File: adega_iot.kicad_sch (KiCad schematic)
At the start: 38 parts, among them J1 Screw_Terminal_01x02, J2 Conn_01x02_Pin, J3 Conn_01x02_Pin, J4 Conn_01x03_Pin, J5 Conn_01x02_Pin, J6 Conn_01x03_Pin, J7 Screw_Terminal_01x02, Q1 IRF540N, Q10 BC548, Q11 BC558, Q2 IRF540N, Q3 BC548, Q4 BC558, Q5 BC548, Q6 BC548, Q7 BC548, Q8 BC558, Q9 BC548, SW1 SW_Push, SW2 SW_Push, U1 RC4558, U2 ESP32-DevKitC

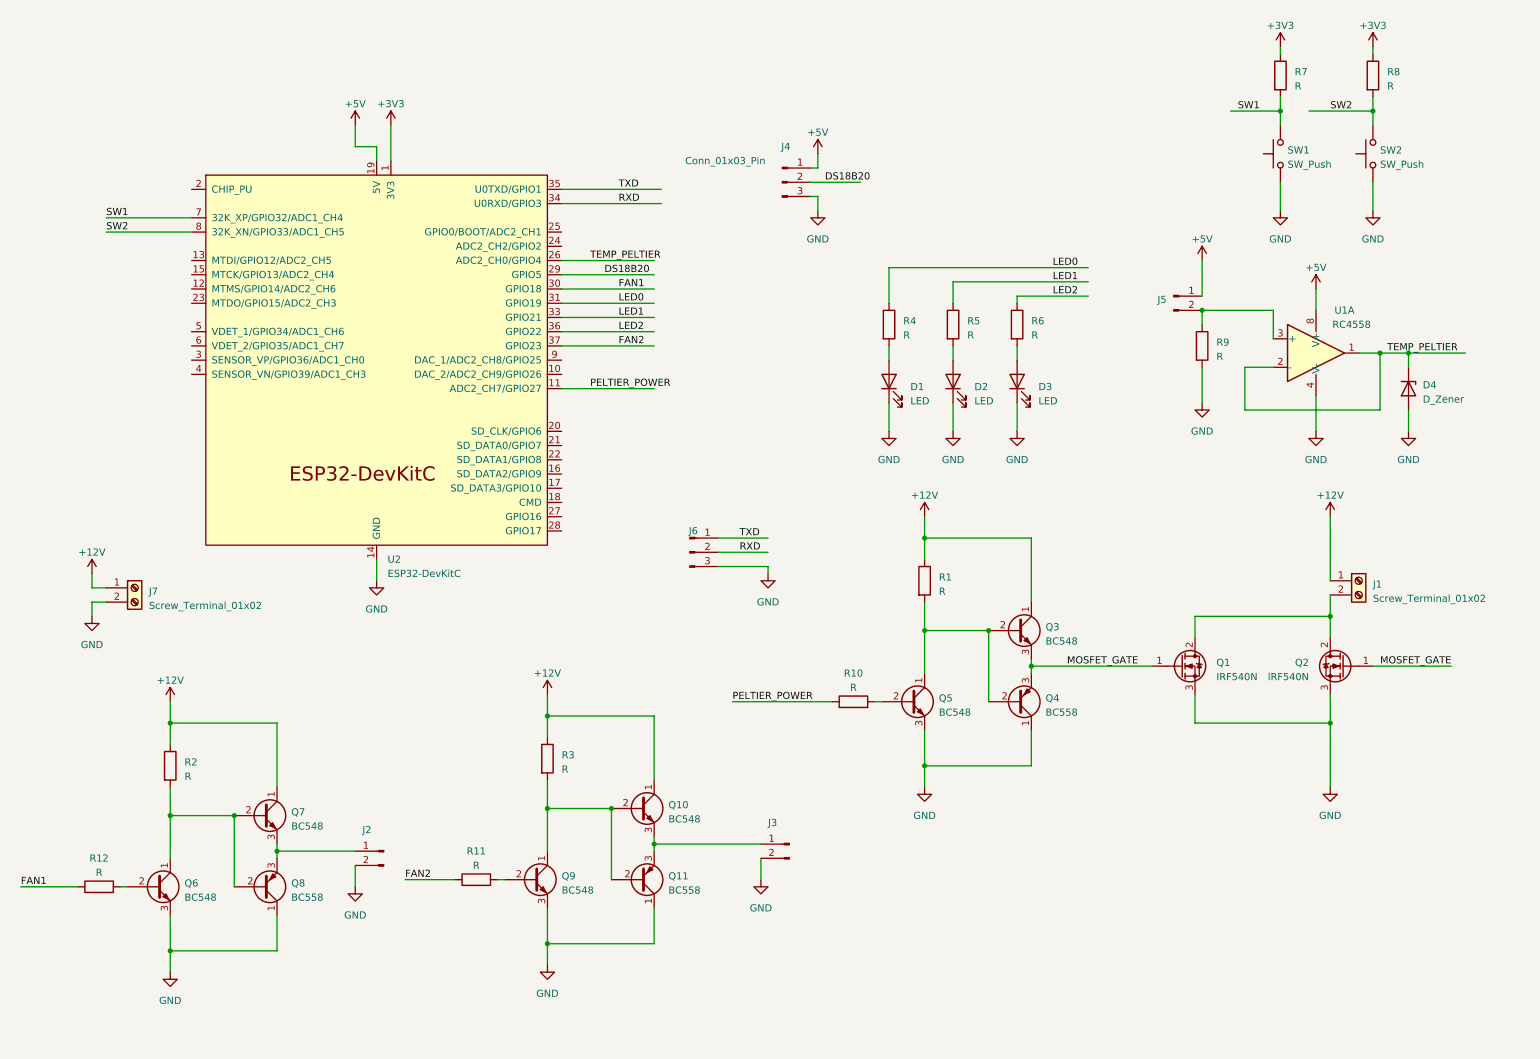
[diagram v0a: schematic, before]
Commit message: Added LM2596
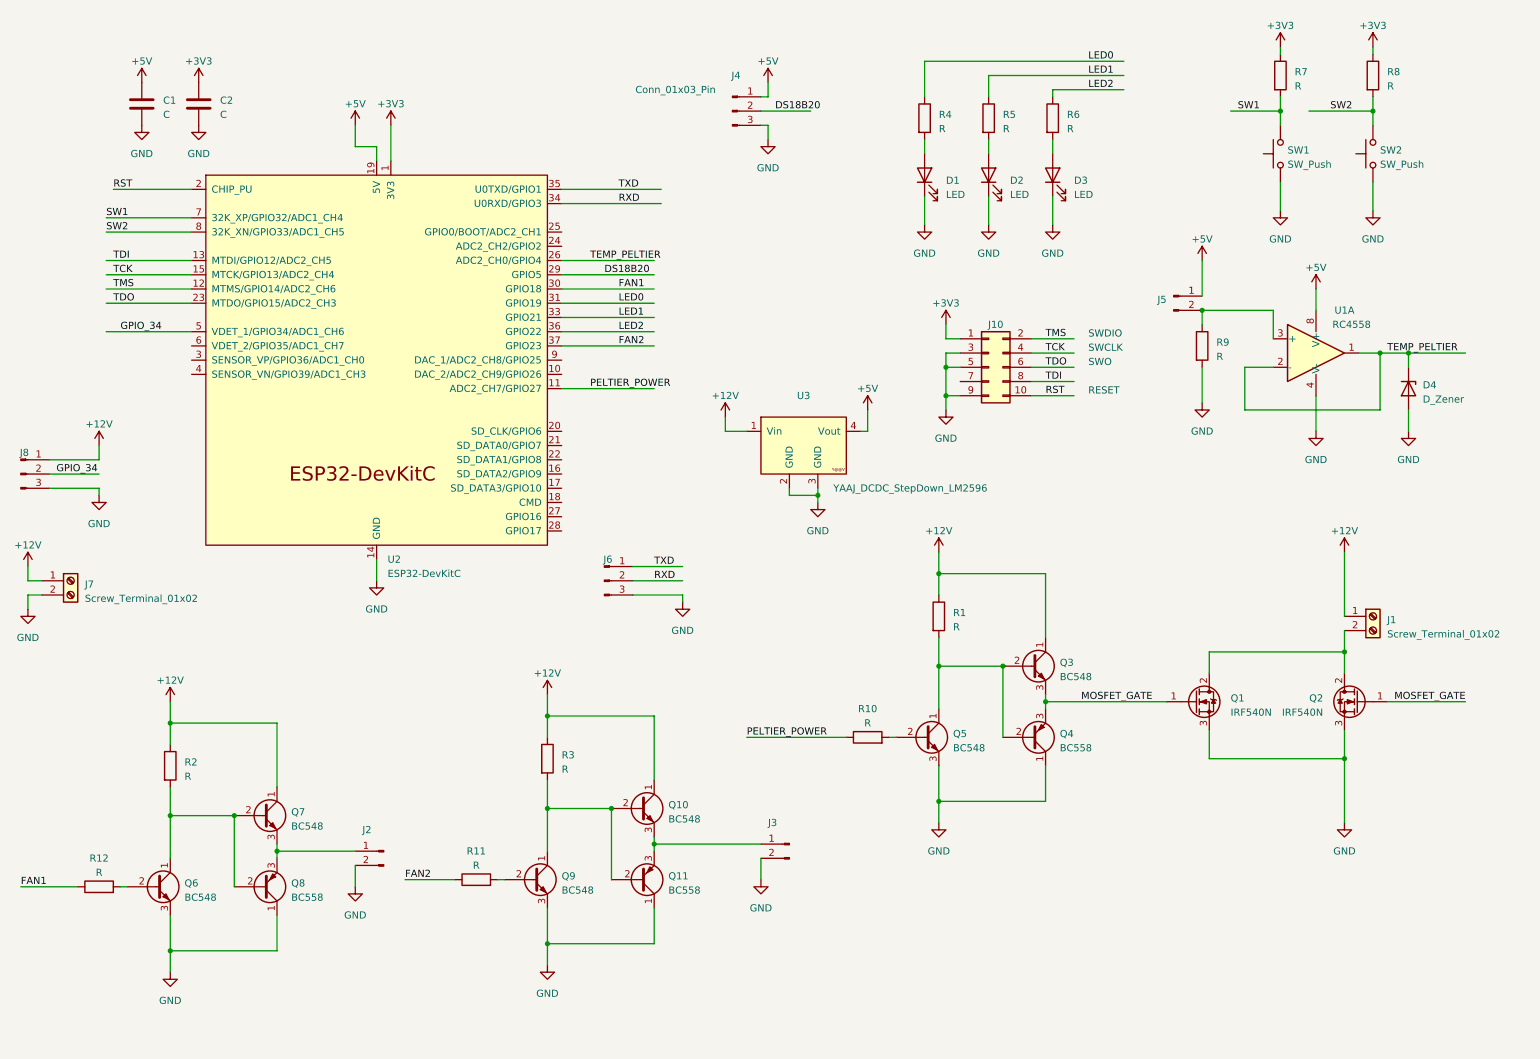
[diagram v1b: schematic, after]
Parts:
- added C1, C2: C, symbol Device:C
- added J10: Conn_02x05_Odd_Even, symbol Connector_Generic:Conn_02x05_Odd_Even
- added J8: Conn_01x03_Pin, symbol Connector:Conn_01x03_Pin
- added U3: YAAJ_DCDC_StepDown_LM2596, lm2596:YAAJ_DCDC_StepDown_LM2596, symbol lm2596:YAAJ_DCDC_StepDown_LM2596
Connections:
- net +12V: now also J8.1 (Pin_1), U3.1 (Vin)
- net +3V3: now also C2.1, J10.1 (Pin_1)
- net +5V: now also C1.1, U3.4 (Vout)
- net GND: now also C1.2, C2.2, J10.3 (Pin_3), J10.5 (Pin_5), J10.9 (Pin_9), J8.3 (Pin_3), U3.2 (GND), U3.3 (GND)
- net TMS: now reaches U2.12 (MTMS/GPIO14/ADC2_CH6)
- net TMS: now also J10.2 (Pin_2)
- net TDI: now reaches U2.13 (MTDI/GPIO12/ADC2_CH5)
- net TDI: now also J10.8 (Pin_8)
- net TCK: now reaches U2.15 (MTCK/GPIO13/ADC2_CH4)
- net TCK: now also J10.4 (Pin_4)
- net RST: now reaches U2.2 (CHIP_PU)
- net RST: now also J10.10 (Pin_10)
- net TDO: now reaches U2.23 (MTDO/GPIO15/ADC2_CH3)
- net TDO: now also J10.6 (Pin_6)
- net GPIO_34: now reaches U2.5 (VDET_1/GPIO34/ADC1_CH6)
- net GPIO_34: now also J8.2 (Pin_2)
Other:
- note added: "RESET"
- note added: "SWCLK"
- note added: "SWDIO"
- note added: "SWO"
- moved on the sheet: D1, D2, D3, J1, J4, J6, J7, Q1, Q2, Q3, Q4, Q5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

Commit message: adding screw terminals
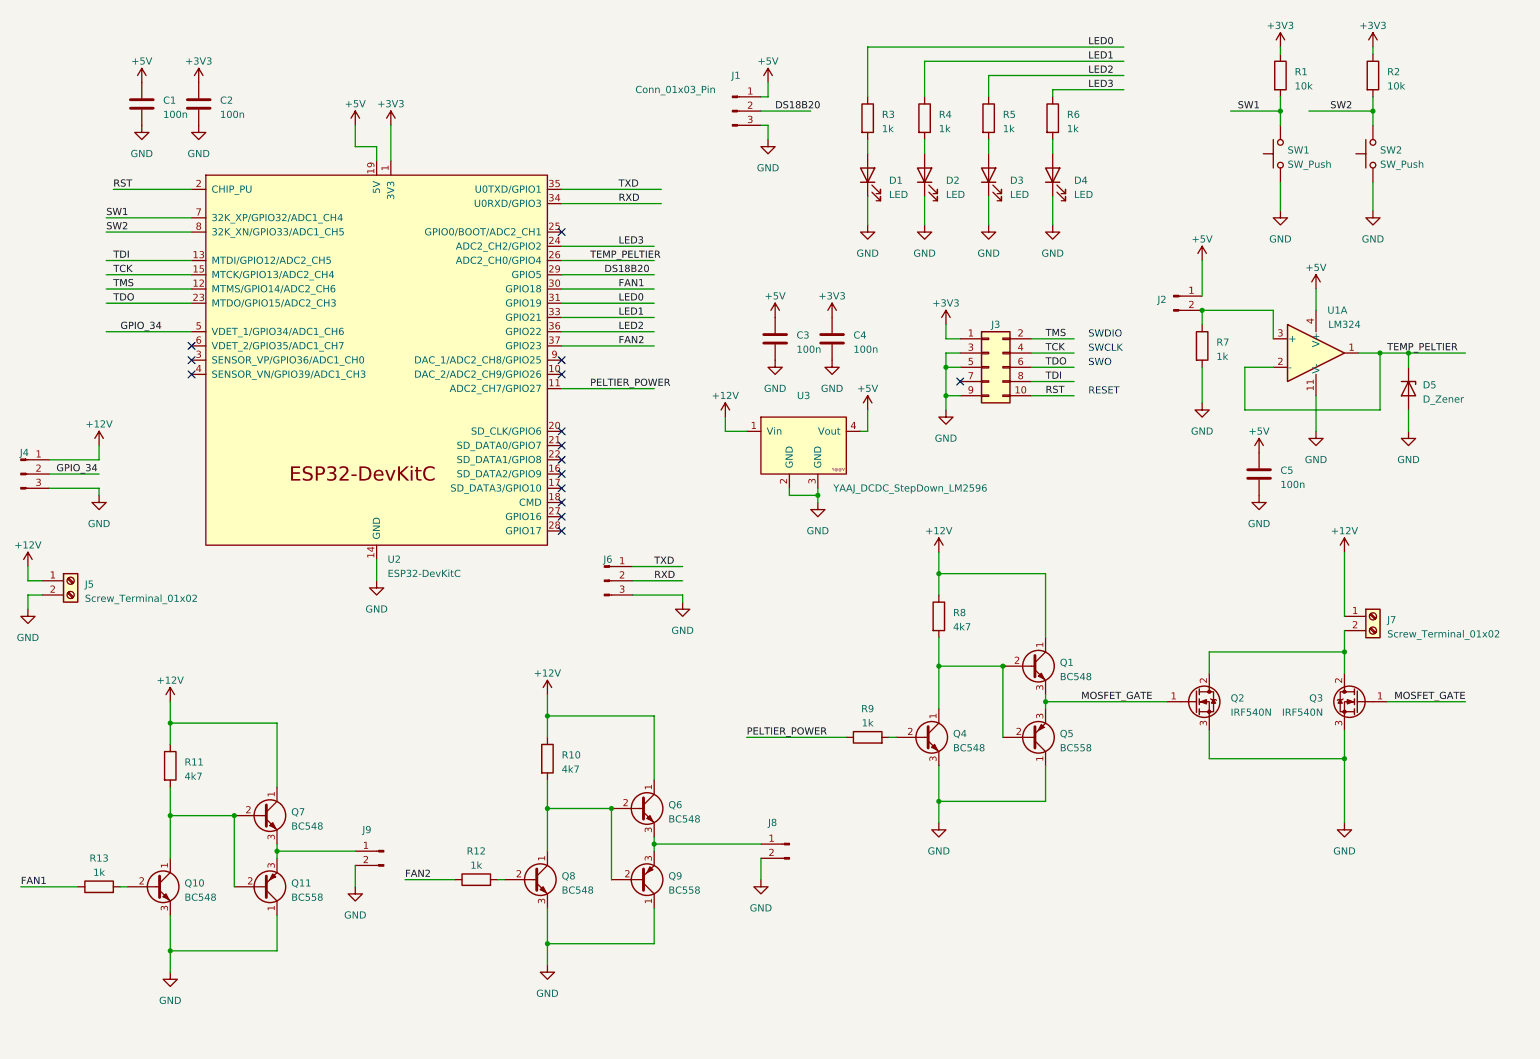
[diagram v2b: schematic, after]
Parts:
- removed U1: RC4558, symbol Amplifier_Operational:RC4558
- added C3, C4, C5: 100n, Capacitor_THT:C_Disc_D7.5mm_W4.4mm_P5.00mm, symbol Device:C
- added D1: LED, LED_THT:LED_D3.0mm, symbol Device:LED
- added R3: 1k, Resistor_THT:R_Axial_DIN0204_L3.6mm_D1.6mm_P7.62mm_Horizontal, symbol Device:R
- added U1: LM324, Package_DIP:DIP-14_W7.62mm, symbol Amplifier_Operational:LM324
- C1, C2: value C -> 100n; footprint (none) -> Capacitor_THT:C_Disc_D7.5mm_W4.4mm_P5.00mm
- D2: renamed from D1; footprint (none) -> LED_THT:LED_D3.0mm
- D3: renamed from D2; footprint (none) -> LED_THT:LED_D3.0mm
- D4: renamed from D3; footprint (none) -> LED_THT:LED_D3.0mm
- D5: renamed from D4; footprint (none) -> Diode_THT:D_A-405_P7.62mm_Horizontal
- J1: renamed from J4; footprint (none) -> Connector_PinHeader_2.54mm:PinHeader_1x03_P2.54mm_Vertical
- J2: renamed from J5; footprint (none) -> Connector_PinHeader_2.54mm:PinHeader_1x02_P2.54mm_Vertical
- J3: renamed from J10; footprint (none) -> Connector_PinHeader_2.54mm:PinHeader_2x05_P2.54mm_Vertical
- J4: renamed from J8; footprint (none) -> Connector_PinHeader_2.54mm:PinHeader_1x03_P2.54mm_Vertical
- J6: footprint (none) -> Connector_PinHeader_2.54mm:PinHeader_1x03_P2.54mm_Vertical
- R1: renamed from R7; value R -> 10k; footprint (none) -> Resistor_THT:R_Axial_DIN0204_L3.6mm_D1.6mm_P7.62mm_Horizontal
- R10: renamed from R3; value R -> 4k7; footprint (none) -> Resistor_THT:R_Axial_DIN0204_L3.6mm_D1.6mm_P7.62mm_Horizontal
- R11: renamed from R2; value R -> 4k7; footprint (none) -> Resistor_THT:R_Axial_DIN0204_L3.6mm_D1.6mm_P7.62mm_Horizontal
- R12: renamed from R11; value R -> 1k; footprint (none) -> Resistor_THT:R_Axial_DIN0204_L3.6mm_D1.6mm_P7.62mm_Horizontal
- R13: renamed from R12; value R -> 1k; footprint (none) -> Resistor_THT:R_Axial_DIN0204_L3.6mm_D1.6mm_P7.62mm_Horizontal
- R2: renamed from R8; value R -> 10k; footprint (none) -> Resistor_THT:R_Axial_DIN0204_L3.6mm_D1.6mm_P7.62mm_Horizontal
- R4, R5, R6: value R -> 1k; footprint (none) -> Resistor_THT:R_Axial_DIN0204_L3.6mm_D1.6mm_P7.62mm_Horizontal
- R7: renamed from R9; value R -> 1k; footprint (none) -> Resistor_THT:R_Axial_DIN0204_L3.6mm_D1.6mm_P7.62mm_Horizontal
- R8: renamed from R1; value R -> 4k7; footprint (none) -> Resistor_THT:R_Axial_DIN0204_L3.6mm_D1.6mm_P7.62mm_Horizontal
- R9: renamed from R10; value R -> 1k; footprint (none) -> Resistor_THT:R_Axial_DIN0204_L3.6mm_D1.6mm_P7.62mm_Horizontal
- renumbered J7 to J5, J1 to J7, J3 to J8, J2 to J9, Q3 to Q1, Q6 to Q10, Q8 to Q11, Q1 to Q2, Q2 to Q3, Q5 to Q4, Q4 to Q5, Q10 to Q6, Q9 to Q8, Q11 to Q9
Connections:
- net +3V3: now also C4.1
- net +5V: now also C3.1, C5.1, U1.4 (V+)
- net GND: now also C3.2, C4.2, C5.2, D1.1 (K), U1.11 (V-)
- net LED0: now also R3.1; no longer R4.1
- net LED1: now also R4.1; no longer R5.1
- net LED2: now also R5.1; no longer R6.1
- net TEMP_PELTIER: now also U1.1, U1.2 (-)
- net at J2.2 (Pin_2), R7.1: now also U1.3 (+)
- net LED3: now reaches U2.24 (ADC2_CH2/GPIO2)
- net LED3: now also R6.1
- new net: D1.2 (A), R3.2
- no-connect marks 0 -> 15

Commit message: Preliminary placement
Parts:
- added F1: Fuse, adega_iot:Metaltex_fuse_holder, symbol Device:Fuse
- J5, J7: footprint (none) -> adega_iot:HANDSON_KF301-2P
- J8, J9: footprint (none) -> Connector_PinHeader_2.54mm:PinHeader_1x02_P2.54mm_Vertical
- Q1, Q10, Q11, Q4, Q5, Q6, Q7, Q8, Q9: footprint Package_TO_SOT_THT:TO-92_Inline -> Package_TO_SOT_THT:TO-92_Inline_Wide
- SW1, SW2: footprint (none) -> Button_Switch_THT:SW_PUSH_6mm_H7.3mm
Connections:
- net +12V: now also F1.1; no longer J5.1 (Pin_1)
- net +3V3: no longer C4.1
- net +5V: now also C4.1
- new net: F1.2, J5.1 (Pin_1)
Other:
- moved on the sheet: C4, J5

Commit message: partial routing
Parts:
- removed C5: 100n, Capacitor_THT:C_Disc_D7.5mm_W4.4mm_P5.00mm, symbol Device:C
- added H1, H10, H11, H12, H2, H3, H4, H5, H6, H7, H8, H9: MountingHole, MountingHole:MountingHole_2mm, symbol Mechanical:MountingHole
- added H13, H14, H15, H16: MountingHole, MountingHole:MountingHole_3.2mm_M3, symbol Mechanical:MountingHole
- added J10: Conn_01x02_Pin, Connector_PinHeader_2.54mm:PinHeader_1x02_P2.54mm_Vertical, symbol Connector:Conn_01x02_Pin
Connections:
- net DS18B20: now also U2.31 (GPIO19); no longer U2.29 (GPIO5)
- net FAN1: now also U2.24 (ADC2_CH2/GPIO2); no longer U2.30 (GPIO18)
- net FAN2: now also U2.29 (GPIO5); no longer U2.37 (GPIO23)
- net GND: now also J10.2 (Pin_2)
- net LED0: now also U2.5 (VDET_1/GPIO34/ADC1_CH6); no longer U2.31 (GPIO19)
- net LED1: now also U2.6 (VDET_2/GPIO35/ADC1_CH7); no longer U2.33 (GPIO21)
- net LED2: now also U2.7 (32K_XP/GPIO32/ADC1_CH4); no longer U2.36 (GPIO22)
- net LED3: now also U2.8 (32K_XN/GPIO33/ADC1_CH5); no longer U2.24 (ADC2_CH2/GPIO2)
- net SW1: now also U2.10 (DAC_2/ADC2_CH9/GPIO26); no longer U2.7 (32K_XP/GPIO32/ADC1_CH4)
- net SW2: now also U2.9 (DAC_1/ADC2_CH8/GPIO25); no longer U2.8 (32K_XN/GPIO33/ADC1_CH5)
- net BOOT: now reaches U2.25 (GPIO0/BOOT/ADC2_CH1)
- net BOOT: now also J10.1 (Pin_1)
- net GPIO_16: now reaches U2.27 (GPIO16)
- net GPIO_16: now also J4.2 (Pin_2)
- removed net GPIO_34: J4.2 (Pin_2), U2.5 (VDET_1/GPIO34/ADC1_CH6)
- no-connect marks 15 -> 8

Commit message: Routing Progress
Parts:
- removed D5: D_Zener, Diode_THT:D_A-405_P7.62mm_Horizontal, symbol Device:D_Zener
- removed J3: Conn_02x05_Odd_Even, Connector_PinHeader_2.54mm:PinHeader_2x05_P2.54mm_Vertical, symbol Connector_Generic:Conn_02x05_Odd_Even
- removed J5: Screw_Terminal_01x02, adega_iot:HANDSON_KF301-2P, symbol Connector:Screw_Terminal_01x02
- added J3: Screw_Terminal_01x02, adega_iot:HANDSON_KF301-2P, symbol Connector:Screw_Terminal_01x02
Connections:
- net +3V3: now also C4.1, J1.1 (Pin_1), J2.1 (Pin_1), U1.4 (V+)
- net +5V: no longer C4.1, J1.1 (Pin_1), J2.1 (Pin_1), U1.4 (V+)
- net GND: now also J3.1 (Pin_1)
- net at F1.2: now also J3.2 (Pin_2)
- no-connect marks 8 -> 7
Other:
- note removed: "RESET"
- note removed: "SWCLK"
- note removed: "SWDIO"
- note removed: "SWO"

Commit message: routing progress
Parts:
- added Q12, Q13: IRF540N, Package_TO_SOT_THT:TO-220-3_Vertical, symbol Transistor_FET:IRF540N
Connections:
- net +12V: now also J8.1 (Pin_1), J9.1 (Pin_1)
- net GND: now also Q12.3 (S), Q13.3 (S); no longer J8.2 (Pin_2), J9.2 (Pin_2)
- net at Q11.3 (E), Q7.3 (E): now also Q13.1 (G); no longer J9.1 (Pin_1)
- net at Q6.3 (E), Q9.3 (E): now also Q12.1 (G); no longer J8.1 (Pin_1)
- new net: J9.2 (Pin_2), Q13.2 (D)
- new net: J8.2 (Pin_2), Q12.2 (D)
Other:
- moved on the sheet: H10, H12, H9, J8, J9
